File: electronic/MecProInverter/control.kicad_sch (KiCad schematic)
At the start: 0 parts

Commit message: electronic
- power: added 3.3V coverter
- power: added bridge rectifier
- power: added half bridge
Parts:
- added U1: TYPE-C_16PIN_2MD(073), footprint:USB-C-SMD_TYPE-C-6PIN-2MD-073, symbol TYPE-C_16PIN_2MD(073):TYPE-C_16PIN_2MD(073)
- added U2: ESP32-S3-MINI-1-N8, ESP32-S3-MINI-1-N8:XCVR_ESP32-S3-MINI-1-N8, symbol ESP32-S3-MINI-1-N8:ESP32-S3-MINI-1-N8
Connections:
- new net: U2.1 (GND), U2.2 (GND), U2.42 (GND), U2.43 (GND), U2.46 (GND), U2.47 (GND), U2.48 (GND), U2.49 (GND), U2.50 (GND), U2.51 (GND), U2.52 (GND), U2.53 (GND), U2.54 (GND), U2.55 (GND), U2.56 (GND), U2.57 (GND), U2.58 (GND), U2.59 (GND), U2.60 (GND), U2.61 (GND), U2.61_1 (GND), U2.61_2 (GND), U2.61_3 (GND), U2.61_4 (GND), U2.61_5 (GND), U2.61_6 (GND), U2.61_7 (GND), U2.61_8 (GND), U2.62 (GND), U2.63 (GND), U2.64 (GND), U2.65 (GND)
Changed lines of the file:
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@@
 (kicad_sch (version 20230121) (generator eeschema)
-  (paper "A4")
+  (paper "A3")
+  (symbol (lib_id "TYPE-C_16PIN_2MD(073):TYPE-C_16PIN_2MD(073)") (at 318.77 69.85 0) (unit 1)
+    (in_bom yes) (on_board yes) (dnp no) (fields_autoplaced)
+    (property "Reference" "U1" (at 318.135 48.26 0)
+      (effects (font (size 1.27 1.27)))
+    )
+    (property "Value" "TYPE-C_16PIN_2MD(073)" (at 318.135 50.8 0)
+      (effects (font (size 1.27 1.27)))
+    )
+    (property "Footprint" "footprint:USB-C-SMD_TYPE-C-6PIN-2MD-073" (at 318.77 80.01 0)
+      (effects (font (size 1.27 1.27) italic) hide)
+    )
+    (property "Datasheet" "https://atta.szlcsc.com/upload/public/pdf/source/20210409/C2765186_34D42616F62DF94D17C4D63D74D9FD03.pdf" (at 316.484 69.723 0)
+      (effects (font (size 1.27 1.27)) (justify left) hide)
+    )
+    (property "LCSC" "C2765186" (at 318.77 69.85 0)
+      (effects (font (size 1.27 1.27)) hide)
+    )
+    (pin "1")
+    (pin "10")
+    (pin "11")
+    (pin "12")
+    (pin "13")
+    (pin "14")
+    (pin "2")
+    (pin "3")
+    (pin "4")
+    (pin "5")
+    (pin "6")
+    (pin "7")
+    (pin "8")
+    (pin "9")
+    (instances
+      (project "MecProInverter"
+        (path "/c9071429-8b0d-45bf-aa6d-71cc2b7f068c/87c5d68c-a194-45d1-987f-2b491b6ac1ab"
+          (reference "U1") (unit 1)
+        )
+      )
+    )
+  )
+  (symbol (lib_id "ESP32-S3-MINI-1-N8:ESP32-S3-MINI-1-N8") (at 83.82 60.96 0) (unit 1)
+    (in_bom yes) (on_board yes) (dnp no) (fields_autoplaced)
+    (property "Reference" "U2" (at 83.82 22.86 0)
+      (effects (font (size 1.27 1.27)))
+    )
+    (property "Value" "ESP32-S3-MINI-1-N8" (at 83.82 25.4 0)
+      (effects (font (size 1.27 1.27)))
+    )
+    (property "Footprint" "ESP32-S3-MINI-1-N8:XCVR_ESP32-S3-MINI-1-N8" (at 83.82 60.96 0)
+      (effects (font (size 1.27 1.27)) (justify bottom) hide)
+    )
+    (property "Datasheet" "" (at 83.82 60.96 0)
+      (effects (font (size 1.27 1.27)) hide)
+    )
+    (property "MF" "Espressif Systems" (at 83.82 60.96 0)
+      (effects (font (size 1.27 1.27)) (justify bottom) hide)
+    )
+    (property "MAXIMUM_PACKAGE_HEIGHT" "2.55mm" (at 83.82 60.96 0)
+      (effects (font (size 1.27 1.27)) (justify bottom) hide)
+    )
+    (property "Package" "None" (at 83.82 60.96 0)
+      (effects (font (size 1.27 1.27)) (justify bottom) hide)
+    )
+    (property "Price" "None" (at 83.82 60.96 0)
+      (effects (font (size 1.27 1.27)) (justify bottom) hide)
+    )
+    (property "Check_prices" "https://www.snapeda.com/parts/ESP32-S3-MINI-1-N8/Espressif+Systems/view-part/?ref=eda" (at 83.82 60.96 0)
+      (effects (font (size 1.27 1.27)) (justify bottom) hide)
+    )
+    (property "STANDARD" "Manufacturer Recommendations" (at 83.82 60.96 0)
+      (effects (font (size 1.27 1.27)) (justify bottom) hide)
+    )
+    (property "PARTREV" "v0.6" (at 83.82 60.96 0)
+      (effects (font (size 1.27 1.27)) (justify bottom) hide)
+    )
+    (property "SnapEDA_Link" "https://www.snapeda.com/parts/ESP32-S3-MINI-1-N8/Espressif+Systems/view-part/?ref=snap" (at 83.82 60.96 0)
+      (effects (font (size 1.27 1.27)) (justify bottom) hide)
+    )
+    (property "MP" "ESP32-S3-MINI-1-N8" (at 83.82 60.96 0)
+      (effects (font (size 1.27 1.27)) (justify bottom) hide)
+    )
+    (property "Purchase-URL" "https://www.snapeda.com/api/url_track_click_mouser/?unipart_id=8941370&manufacturer=Espressif Systems&part_name=ESP32-S3-MINI-1-N8&search_term=None" (at 83.82 60.96 0)
+      (effects (font (size 1.27 1.27)) (justify bottom) hide)
+    )
+    (property "Description" "\nBluetooth, WiFi 802.11b/g/n, Bluetooth v5.0 Transceiver Module 2.4GHz PCB Trace Surface Mount\n" (at 83.82 60.96 0)
+      (effects (font (size 1.27 1.27)) (justify bottom) hide)
+    )
+    (property "Availability" "In Stock" (at 83.82 60.96 0)
+      (effects (font (size 1.27 1.27)) (justify bottom) hide)
+    )
+    (property "MANUFACTURER" "Espressif" (at 83.82 60.96 0)
+      (effects (font (size 1.27 1.27)) (justify bottom) hide)
+    )
+    (pin "1")
+    (pin "10")
+    (pin "11")
+    (pin "12")
+    (pin "13")
+    (pin "14")
+    (pin "15")
+    (pin "16")
+    (pin "17")
+    (pin "18")
+    (pin "19")
+    (pin "2")
+    (pin "20")
+    (pin "21")
+    (pin "22")
+    (pin "23")
+    (pin "24")
+    (pin "25")
+    (pin "26")
+    (pin "27")
+    (pin "28")
+    (pin "29")
+    (pin "3")
+    (pin "30")
+    (pin "31")
+    (pin "32")
+    (pin "33")
+    (pin "34")
+    (pin "35")
+    (pin "36")
+    (pin "37")
+    (pin "38")
+    (pin "39")
+    (pin "4")
+    (pin "40")
+    (pin "41")
+    (pin "42")
+    (pin "43")
+    (pin "44")
+    (pin "45")
+    (pin "46")
+    (pin "47")
+    (pin "48")
+    (pin "49")
+    (pin "5")
+    (pin "50")
+    (pin "51")
+    (pin "52")
+    (pin "53")
+    (pin "54")
+    (pin "55")
+    (pin "56")
+    (pin "57")
+    (pin "58")
+    (pin "59")
+    (pin "6")
+    (pin "60")
+    (pin "61")
+    (pin "61_1")
+    (pin "61_2")
+    (pin "61_3")
+    (pin "61_4")
+    (pin "61_5")
+    (pin "61_6")
+    (pin "61_7")
+    (pin "61_8")
+    (pin "62")
+    (pin "63")
+    (pin "64")
+    (pin "65")
+    (pin "7")
+    (pin "8")
+    (pin "9")
+    (instances
+      (project "MecProInverter"
+        (path "/c9071429-8b0d-45bf-aa6d-71cc2b7f068c/87c5d68c-a194-45d1-987f-2b491b6ac1ab"
+          (reference "U2") (unit 1)
+        )
+      )
+    )
+  )
 )

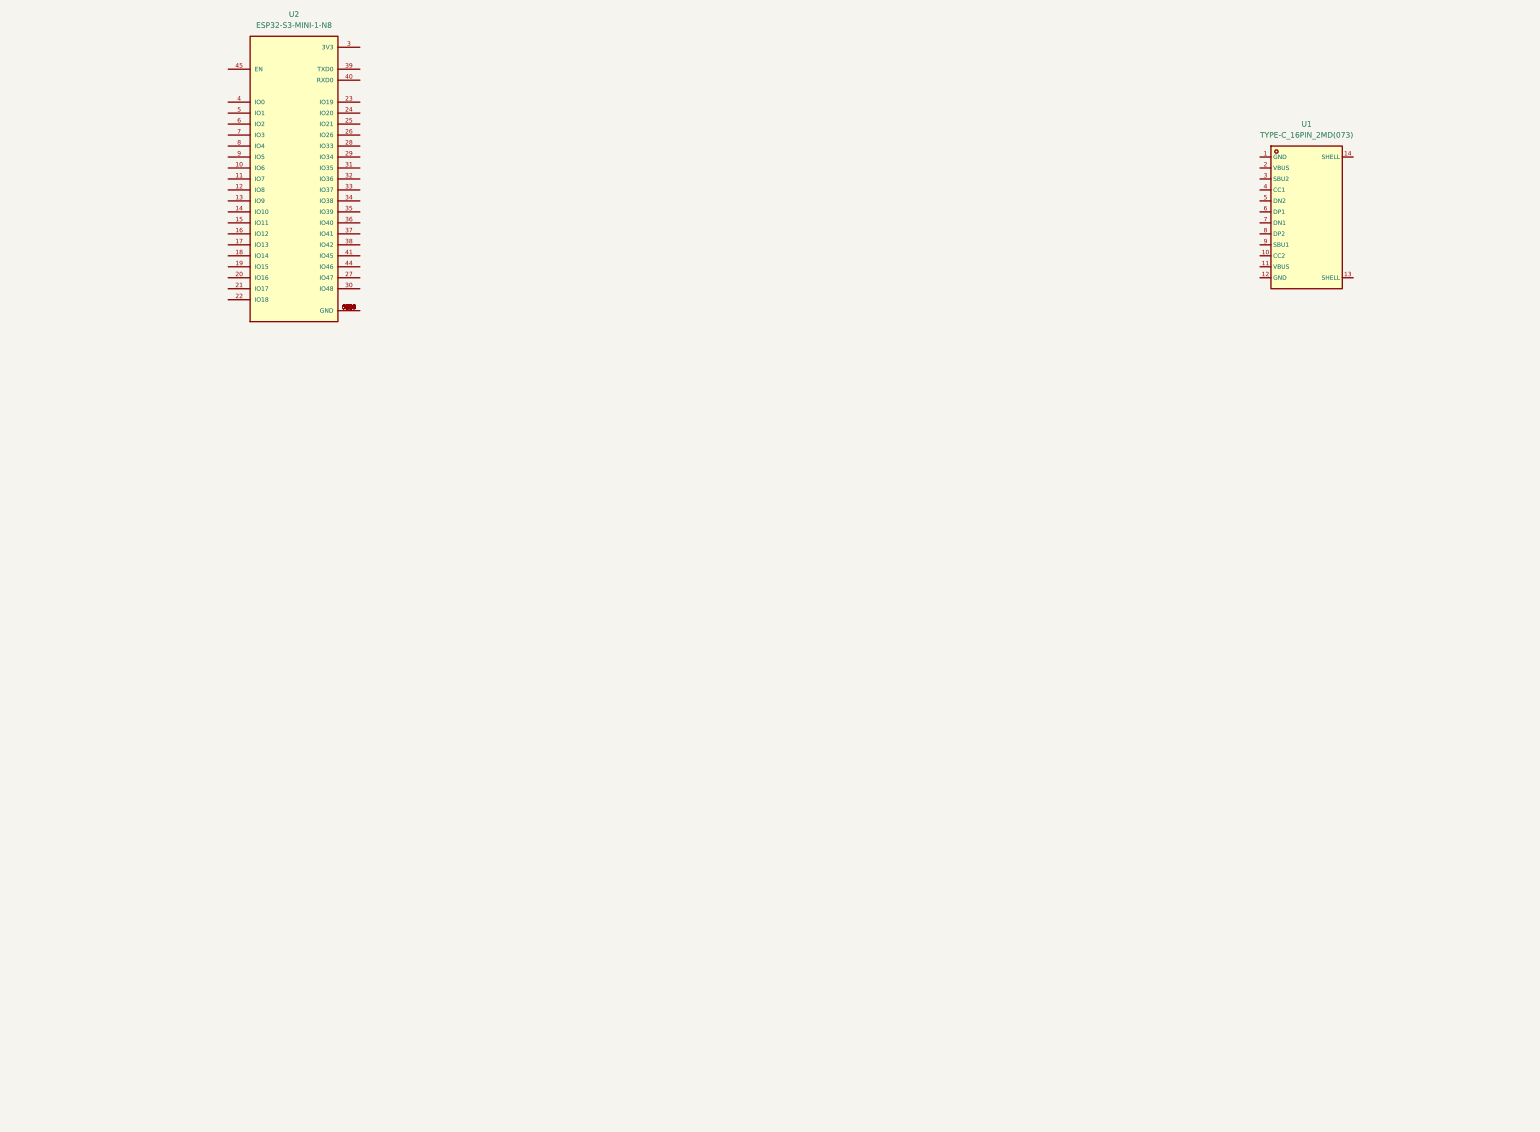
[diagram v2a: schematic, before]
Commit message: electronic
-power: added 15/3,3 Volt voltage regulator
- power: added power relay
- control: added USB-ISO, added User interface
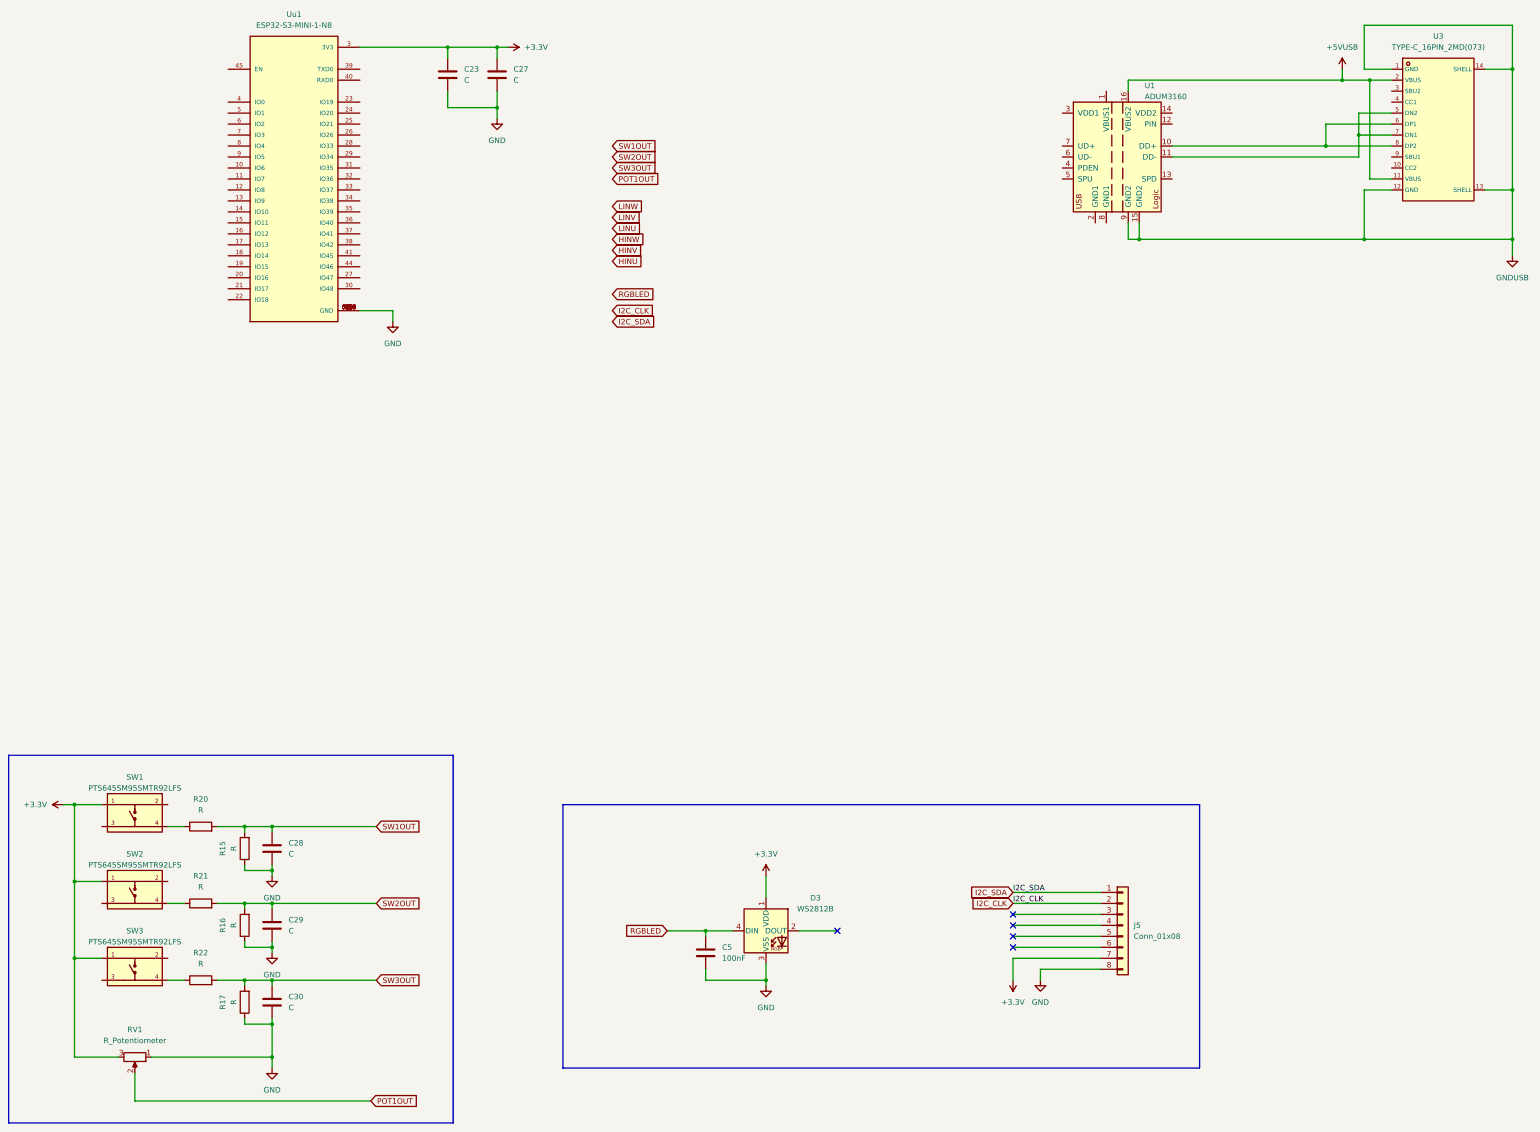
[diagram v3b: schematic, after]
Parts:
- added C23, C27, C28, C29, C30: C, symbol Device:C
- added C5: 100nF, symbol Device:C
- added D3: WS2812B, LED_SMD:LED_WS2812B_PLCC4_5.0x5.0mm_P3.2mm, symbol LED:WS2812B
- added J5: Conn_01x08, symbol Connector_Generic:Conn_01x08
- added R15, R16, R17, R20, R21, R22: R, symbol Device:R
- added RV1: R_Potentiometer, symbol Device:R_Potentiometer
- added SW1, SW2, SW3: PTS645SM95SMTR92LFS, footprint:KEY-SMD_4P-L6.1-W6.1-P4.50-LS9.0, symbol PTS645SM95SMTR92LFS:PTS645SM95SMTR92LFS
- added U1: ADUM3160, Package_SO:SOIC-16W_7.5x10.3mm_P1.27mm, symbol Interface_USB:ADUM3160
- renumbered U1 to U3, U2 to Uu1
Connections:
- net GND: now reaches U3.1 (GND)
- net GND: now also U3.12 (GND), U3.13 (SHELL), U3.14 (SHELL), Uu1.1 (GND), Uu1.2 (GND), Uu1.42 (GND), Uu1.43 (GND), Uu1.46 (GND), Uu1.47 (GND), Uu1.48 (GND), Uu1.49 (GND), Uu1.50 (GND), Uu1.51 (GND), Uu1.52 (GND), Uu1.53 (GND), Uu1.54 (GND), Uu1.55 (GND), Uu1.56 (GND), Uu1.57 (GND), Uu1.58 (GND), Uu1.59 (GND), Uu1.60 (GND), Uu1.61 (GND), Uu1.61_1 (GND), Uu1.61_2 (GND), Uu1.61_3 (GND), Uu1.61_4 (GND), Uu1.61_5 (GND), Uu1.61_6 (GND), Uu1.61_7 (GND), Uu1.61_8 (GND), Uu1.62 (GND), Uu1.63 (GND), Uu1.64 (GND), Uu1.65 (GND), C23.2, C27.2, C28.2, C29.2, C30.2, C5.2, D3.3 (VSS), J5.8 (Pin_8), R15.1, R16.1, R17.1, RV1.1, U1.15 (GND2), U1.9 (GND2)
- net +5V: now reaches U3.11 (VBUS)
- net +5V: now also U3.2 (VBUS), U1.16 (VBUS2)
- net at U3.5 (DN2): now also U3.7 (DN1), U1.11 (DD-)
- net at U3.6 (DP1): now also U3.8 (DP2), U1.10 (DD+)
- net +3.3V: now reaches Uu1.3 (3V3)
- net +3.3V: now also C23.1, C27.1, D3.1 (VDD), J5.7 (Pin_7), RV1.3, SW1.1, SW2.1, SW3.1
- new net: R21.1, SW2.4
- new net: R22.1, SW3.4
- new net: R20.1, SW1.4
- new net I2C_CLK: J5.2 (Pin_2)
- new net I2C_SDA: J5.1 (Pin_1)
- new net POT1OUT: RV1.2
- new net RGBLED: C5.1, D3.4 (DIN)
- new net SW1OUT: C28.1, R15.2, R20.2
- new net SW2OUT: C29.1, R16.2, R21.2
- new net SW3OUT: C30.1, R17.2, R22.2
- no-connect marks 0 -> 5
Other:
- moved on the sheet: U3

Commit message: electronic
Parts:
- added C31, C7: 1uF, symbol Device:C
- added R23: 100K, symbol Device:R
- added R24, R25: 4.75K, symbol Device:R
- added R26, R27: 121, symbol Device:R
- added U6, U7: SKRKAEE020, footprint:SW-SMD_L3.9-W3.0-P4.45, symbol SKRKAEE020:SKRKAEE020
- C23: value C -> 100nF
- C27: value C -> 22uF
- C28, C29, C30: value C -> 1uF
- R15, R16, R17: value R -> 100K
- R20, R21: value R -> 1K
- R22: value R -> 1k
- RV1: value R_Potentiometer -> 10K
- renumbered Uu1 to U1, U1 to U2
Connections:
- net +3.3V: now also U2.16 (VBUS2), R23.1, R24.1, R25.2
- net +5V: now also U2.1 (VBUS1); no longer U2.16 (VBUS2)
- net GND: now also U2.2 (GND1), U2.8 (GND1), C31.2, C7.2, U6.1, U7.1
- net HINU: now also U1.18 (IO14)
- net HINV: now also U1.17 (IO13)
- net HINW: now also U1.16 (IO12)
- net I2C_CLK: now also U1.22 (IO18), R25.1, R27.1; no longer J5.2 (Pin_2)
- net I2C_SDA: now also U1.21 (IO17), R24.2, R26.1; no longer J5.1 (Pin_1)
- net LINU: now also U1.15 (IO11)
- net LINV: now also U1.14 (IO10)
- net LINW: now also U1.13 (IO9)
- net POT1OUT: now also U1.11 (IO7)
- net RGBLED: now also U1.12 (IO8)
- net SW1OUT: now also U1.8 (IO4)
- net SW2OUT: now also U1.9 (IO5)
- net SW3OUT: now also U1.10 (IO6)
- net at U3.6 (DP1), U3.8 (DP2): now also U2.7 (UD+); no longer U2.10 (DD+)
- net at U3.5 (DN2), U3.7 (DN1): now also U2.6 (UD-); no longer U2.11 (DD-)
- net USB_DN: now reaches U1.23 (IO19)
- net USB_DN: now also U2.11 (DD-)
- net USB_DP: now reaches U1.24 (IO20)
- net USB_DP: now also U2.10 (DD+)
- net at U1.4 (IO0): now also C31.1, U6.2
- net at U1.45 (EN): now also C7.1, R23.2, U7.2
- new net: J5.2 (Pin_2), R27.2
- new net: J5.1 (Pin_1), R26.2
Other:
- moved on the sheet: C23, C27, C5, U1, U2, U3
